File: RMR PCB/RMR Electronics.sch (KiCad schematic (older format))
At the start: 6 parts, among them J1 Conn_01x02_Female

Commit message: V1 of the pcb design
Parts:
- removed R1, R?: R, symbol R
- added B1, B2: 18650mount, symbol 18650mount
- added C3: 0.33uf, symbol CP
- added C4: 0.1uf, symbol CP
- added J2: Arduino Power, symbol Conn_01x02_Female
- added J3: Left Servo, symbol Conn_01x02_Female
- added J4: Right Servo, symbol Conn_01x02_Female
- added J5: Mast Servo, symbol Conn_01x02_Female
- added U2: LD1117S18TR_SOT223, TO_SOT_Packages_SMD:SOT-223-3Lead_TabPin2, symbol LD1117S18TR_SOT223
- C1: value 0.1uf -> 0.33uf
- C2: value 1uf -> 0.1uf
- J1: value Conn_01x02_Female -> RasPi Power
- gave numbers to parts that had none: 1
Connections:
- net GND: now also U1.1 (GND), B1.~ (-ve), B2.~ (-ve), C3.2, C4.2, J2.1 (Pin_1), J3.1 (Pin_1), J4.1 (Pin_1), J5.1 (Pin_1), U2.1 (GND)
- net at C1.1, U1.3 (VI): now also B1.~ (-ve), B2.~ (-ve), C3.1, J2.2 (Pin_2), U2.3 (VI)
- new net: C4.1, J3.2 (Pin_2), J4.2 (Pin_2), J5.2 (Pin_2), U2.2 (VO)
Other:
- moved on the sheet: C2

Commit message: Modifications for the night
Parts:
- added D1: LED, symbol LED
- added R1: 220, symbol R
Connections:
- new net: B1.~ (-ve), B2.~ (-ve), C1.1, D1.1 (K), J2.2 (Pin_2), U1.3 (VI)
- new net: C3.1, R1.1, U2.3 (VI)
- new net: D1.2 (A), R1.2
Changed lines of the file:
@@
 $EndComp
 $Comp
-L GND #PWR?
+L GND #PWR01
 U 1 1 5B1ABB87
 P 3100 2200
-F 0 "#PWR?" H 3100 1950 50  0001 C CNN
+F 0 "#PWR01" H 3100 1950 50  0001 C CNN
 F 1 "GND" H 3100 2050 50  0000 C CNN
 F 2 "" H 3100 2200 50  0001 C CNN
@@
 $EndComp
 $Comp
-L GND #PWR?
+L GND #PWR02
 U 1 1 5B1ABBCB
 P 3800 3450
-F 0 "#PWR?" H 3800 3200 50  0001 C CNN
+F 0 "#PWR02" H 3800 3200 50  0001 C CNN
 F 1 "GND" H 3800 3300 50  0000 C CNN
 F 2 "" H 3800 3450 50  0001 C CNN
@@
 $EndComp
 $Comp
-L GND #PWR?
+L GND #PWR03
 U 1 1 5B1B3E95
 P 2650 2550
-F 0 "#PWR?" H 2650 2300 50  0001 C CNN
+F 0 "#PWR03" H 2650 2300 50  0001 C CNN
 F 1 "GND" H 2650 2400 50  0000 C CNN
 F 2 "" H 2650 2550 50  0001 C CNN
@@
 $EndComp
 $Comp
-L GND #PWR?
+L GND #PWR04
 U 1 1 5B1B4450
 P 5000 3600
-F 0 "#PWR?" H 5000 3350 50  0001 C CNN
+F 0 "#PWR04" H 5000 3350 50  0001 C CNN
 F 1 "GND" H 5000 3450 50  0000 C CNN
 F 2 "" H 5000 3600 50  0001 C CNN
@@
 $EndComp
 $Comp
-L GND #PWR?
+L GND #PWR05
 U 1 1 5B1B4605
 P 4650 2050
-F 0 "#PWR?" H 4650 1800 50  0001 C CNN
+F 0 "#PWR05" H 4650 1800 50  0001 C CNN
 F 1 "GND" H 4650 1900 50  0000 C CNN
 F 2 "" H 4650 2050 50  0001 C CNN
@@
 $EndComp
 $Comp
-L GND #PWR?
+L GND #PWR06
 U 1 1 5B1B463B
 P 5100 1950
-F 0 "#PWR?" H 5100 1700 50  0001 C CNN
+F 0 "#PWR06" H 5100 1700 50  0001 C CNN
 F 1 "GND" H 5100 1800 50  0000 C CNN
 F 2 "" H 5100 1950 50  0001 C CNN
@@
 $EndComp
 $Comp
-L GND #PWR?
+L GND #PWR07
 U 1 1 5B1B466A
 P 5550 1950
-F 0 "#PWR?" H 5550 1700 50  0001 C CNN
+F 0 "#PWR07" H 5550 1700 50  0001 C CNN
 F 1 "GND" H 5550 1800 50  0000 C CNN
 F 2 "" H 5550 1950 50  0001 C CNN
@@
 Wire Wire Line
 	3100 2850 3100 3700
-Wire Wire Line
-	3100 3700 4700 3700
 Connection ~ 3100 2850
-Wire Wire Line
-	4700 3700 4700 2850
 Connection ~ 4700 3450
 Wire Wire Line
@@
 Connection ~ 3100 3250
 $Comp
-L GND #PWR?
+L GND #PWR08
 U 1 1 5B1B491C
 P 2750 3000
-F 0 "#PWR?" H 2750 2750 50  0001 C CNN
+F 0 "#PWR08" H 2750 2750 50  0001 C CNN
 F 1 "GND" H 2750 2850 50  0000 C CNN
 F 2 "" H 2750 3000 50  0001 C CNN
@@
 $EndComp
 $Comp
-L GND #PWR?
+L GND #PWR09
 U 1 1 5B1B49DF
 P 2750 3400
-F 0 "#PWR?" H 2750 3150 50  0001 C CNN
+F 0 "#PWR09" H 2750 3150 50  0001 C CNN
 F 1 "GND" H 2750 3250 50  0000 C CNN
 F 2 "" H 2750 3400 50  0001 C CNN
@@
 Wire Wire Line
 	2550 3400 2750 3400
+$Comp
+L LED D1
+U 1 1 5B1B4CC6
+P 3450 3700
+F 0 "D1" H 3450 3800 50  0000 C CNN
+F 1 "LED" H 3450 3600 50  0000 C CNN
+F 2 "" H 3450 3700 50  0001 C CNN
+F 3 "" H 3450 3700 50  0001 C CNN
+	1    3450 3700
+	1    0    0    -1
+$EndComp
+$Comp
+L R R1
+U 1 1 5B1B4D43
+P 3850 3700
+F 0 "R1" V 3930 3700 50  0000 C CNN
+F 1 "220" V 3850 3700 50  0000 C CNN
+F 2 "" V 3780 3700 50  0001 C CNN
+F 3 "" H 3850 3700 50  0001 C CNN
+	1    3850 3700
+	0    1    1    0
+$EndComp
+Wire Wire Line
+	3100 3700 3300 3700
+Wire Wire Line
+	3600 3700 3700 3700
+Wire Wire Line
+	4700 3700 4000 3700
+Wire Wire Line
+	4700 2850 4700 3700
 $EndSCHEMATC

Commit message: Finished layout
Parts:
- removed J1: RasPi Power, symbol Conn_01x02_Female
- removed J2: Arduino Power, symbol Conn_01x02_Female
- removed J3: Left Servo, symbol Conn_01x02_Female
- removed J4: Right Servo, symbol Conn_01x02_Female
- removed J5: Mast Servo, symbol Conn_01x02_Female
- added C5: 100 uf, symbol CP
- added H1: HBridge, symbol HBridge
- added J1: Arduino Power, symbol Conn_01x02_Male
- added J2: RPI Power, symbol Conn_01x02_Male
- added J3: Mast Servo, symbol Conn_01x03_Male
- added J4: RMotor, symbol Conn_01x02_Male
- added J5: LMotor, symbol Conn_01x02_Male
- added J6: Conn_01x01_Male, symbol Conn_01x01_Male
- added J7: LMotor Control, symbol Conn_01x02_Male
- added J8: RMotor Control, symbol Conn_01x02_Male
- R1: value 220 -> R
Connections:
- net GND: now also C5.2, H1.~ (VCC2), J1.2 (Pin_2), J2.2 (Pin_2), J3.3 (Pin_3); no longer B1.~ (-ve)
- net at C2.1, U1.2 (VO): now also J2.1 (Pin_1)
- net at C4.1, U2.2 (VO): now also R1.2
- net at C3.1, U2.3 (VI): now also B1.~ (-ve), C1.1, U1.3 (VI), J1.1 (Pin_1); no longer R1.1
- net at D1.2 (A): now also R1.1; no longer R1.2
- new net: B1.~ (-ve), B2.~ (-ve)
- new net: C5.1, D1.1 (K), H1.~ (VCC2), J3.1 (Pin_1)
- new net: J3.2 (Pin_2), J6.1 (Pin_1)
- new net: H1.~ (VCC2), J8.1 (Pin_1)
- new net: H1.~ (VCC2), J8.2 (Pin_2)
- new net: H1.~ (VCC2), J7.1 (Pin_1)
- new net: H1.~ (VCC2), J7.2 (Pin_2)
- new net: H1.~ (VCC2), J4.1 (Pin_1)
- new net: H1.~ (VCC2), J4.2 (Pin_2)
- new net: H1.~ (VCC2), J5.1 (Pin_1)
- new net: H1.~ (VCC2), J5.2 (Pin_2)

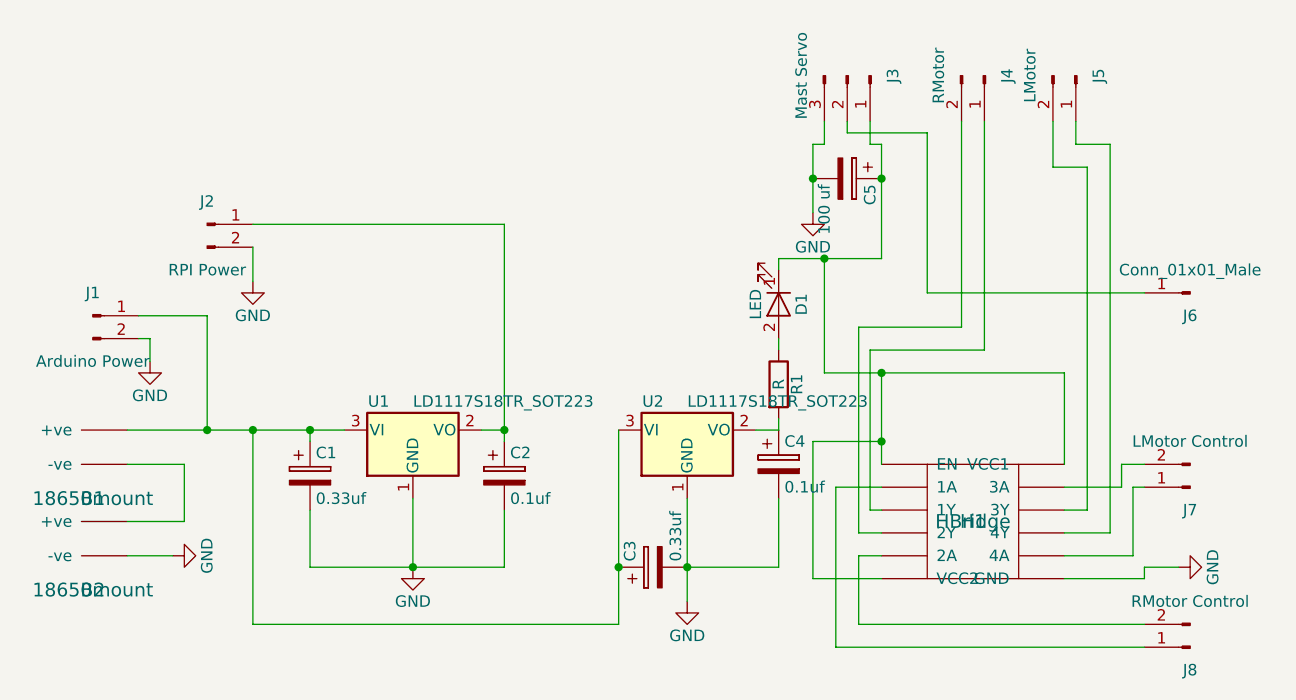
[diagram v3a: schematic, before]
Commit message: added footprints
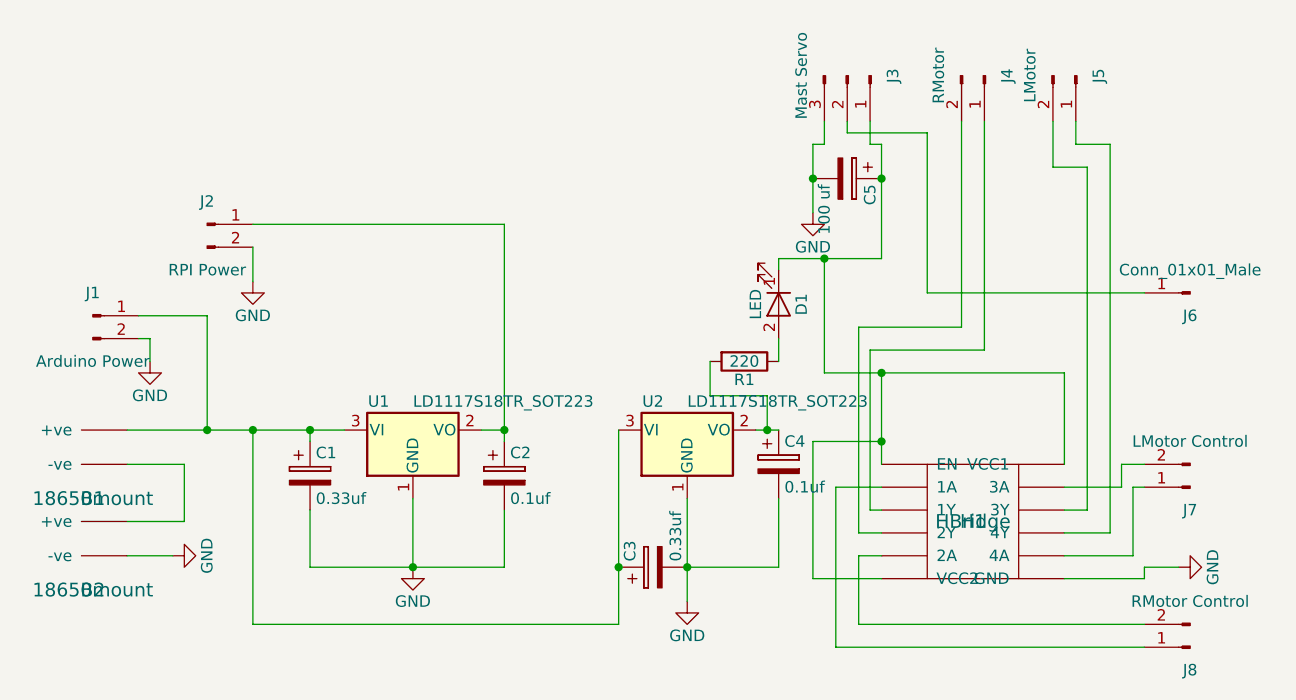
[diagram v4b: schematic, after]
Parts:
- J1, J2, J4, J5, J7, J8: footprint (none) -> Pin_Headers:Pin_Header_Straight_1x02_Pitch2.54mm
- J3: footprint (none) -> Pin_Headers:Pin_Header_Straight_1x03_Pitch2.54mm
- J6: footprint (none) -> Pin_Headers:Pin_Header_Straight_1x01_Pitch2.54mm
- R1: value R -> 220
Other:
- moved on the sheet: R1
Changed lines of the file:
@@
 F 0 "J3" H 5700 1500 50  0000 C CNN
 F 1 "Mast Servo" H 5700 1100 50  0000 C CNN
-F 2 "" H 5700 1300 50  0001 C CNN
+F 2 "Pin_Headers:Pin_Header_Straight_1x03_Pitch2.54mm" H 5700 1300 50  0001 C CNN
 F 3 "" H 5700 1300 50  0001 C CNN
 	1    5700 1300
@@
 F 0 "J8" H 7200 3900 50  0000 C CNN
 F 1 "RMotor Control" H 7200 3600 50  0000 C CNN
-F 2 "" H 7200 3800 50  0001 C CNN
+F 2 "Pin_Headers:Pin_Header_Straight_1x02_Pitch2.54mm" H 7200 3800 50  0001 C CNN
 F 3 "" H 7200 3800 50  0001 C CNN
 	1    7200 3800
@@
 Connection ~ 5000 3450
 Wire Wire Line
-	5400 2850 5300 2850
+	5300 2850 5400 2850
 Wire Wire Line
 	2550 3400 2750 3400
@@
 F 0 "J7" H 7200 3200 50  0000 C CNN
 F 1 "LMotor Control" H 7200 2900 50  0000 C CNN
-F 2 "" H 7200 3100 50  0001 C CNN
+F 2 "Pin_Headers:Pin_Header_Straight_1x02_Pitch2.54mm" H 7200 3100 50  0001 C CNN
 F 3 "" H 7200 3100 50  0001 C CNN
 	1    7200 3100
@@
 F 0 "J4" H 6300 1400 50  0000 C CNN
 F 1 "RMotor" H 6300 1100 50  0000 C CNN
-F 2 "" H 6300 1300 50  0001 C CNN
+F 2 "Pin_Headers:Pin_Header_Straight_1x02_Pitch2.54mm" H 6300 1300 50  0001 C CNN
 F 3 "" H 6300 1300 50  0001 C CNN
 	1    6300 1300
@@
 F 0 "J5" H 6700 1400 50  0000 C CNN
 F 1 "LMotor" H 6700 1100 50  0000 C CNN
-F 2 "" H 6700 1300 50  0001 C CNN
+F 2 "Pin_Headers:Pin_Header_Straight_1x02_Pitch2.54mm" H 6700 1300 50  0001 C CNN
 F 3 "" H 6700 1300 50  0001 C CNN
 	1    6700 1300
@@
 F 0 "J6" H 7200 2350 50  0000 C CNN
 F 1 "Conn_01x01_Male" H 7200 2150 50  0000 C CNN
-F 2 "" H 7200 2250 50  0001 C CNN
+F 2 "Pin_Headers:Pin_Header_Straight_1x01_Pitch2.54mm" H 7200 2250 50  0001 C CNN
 F 3 "" H 7200 2250 50  0001 C CNN
 	1    7200 2250
@@
 L R R1
 U 1 1 5B3D53C2
-P 5400 2650
-F 0 "R1" V 5480 2650 50  0000 C CNN
-F 1 "R" V 5400 2650 50  0000 C CNN
-F 2 "" V 5330 2650 50  0001 C CNN
-F 3 "" H 5400 2650 50  0001 C CNN
-	1    5400 2650
-	1    0    0    -1
-$EndComp
-Wire Wire Line
-	5400 2800 5400 2850
+P 5250 2550
+F 0 "R1" V 5330 2550 50  0000 C CNN
+F 1 "220" V 5250 2550 50  0000 C CNN
+F 2 "" V 5180 2550 50  0001 C CNN
+F 3 "" H 5250 2550 50  0001 C CNN
+	1    5250 2550
+	0    1    1    0
+$EndComp
 $Comp
 L LED D1
@@
 	5400 2100 5400 2150
 Wire Wire Line
-	5400 2450 5400 2500
-Wire Wire Line
 	5600 2100 5600 2600
 Connection ~ 5600 2100
@@
 F 0 "J2" H 2900 2050 50  0000 C CNN
 F 1 "RPI Power" H 2900 1750 50  0000 C CNN
-F 2 "" H 2900 1950 50  0001 C CNN
+F 2 "Pin_Headers:Pin_Header_Straight_1x02_Pitch2.54mm" H 2900 1950 50  0001 C CNN
 F 3 "" H 2900 1950 50  0001 C CNN
 	1    2900 1950
@@
 F 0 "J1" H 2400 2450 50  0000 C CNN
 F 1 "Arduino Power" H 2400 2150 50  0000 C CNN
-F 2 "" H 2400 2350 50  0001 C CNN
+F 2 "Pin_Headers:Pin_Header_Straight_1x02_Pitch2.54mm" H 2400 2350 50  0001 C CNN
 F 3 "" H 2400 2350 50  0001 C CNN
 	1    2400 2350
@@
 Wire Wire Line
 	3800 3150 3800 3450
+Wire Wire Line
+	5350 2850 5350 2700
+Wire Wire Line
+	5350 2700 5100 2700
+Wire Wire Line
+	5100 2700 5100 2550
+Connection ~ 5350 2850
+Wire Wire Line
+	5400 2550 5400 2450
 $EndSCHEMATC
